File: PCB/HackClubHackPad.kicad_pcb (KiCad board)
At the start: 2 copper layers, 59.1 x 47 mm, 7 parts, among them J1 Conn_01x04, SW1 SW_Push, SW2 SW_Push, SW3 SW_Push, SW4 RotaryEncoder_Switch, SW5 RotaryEncoder_Switch, U1 Seeed Studio XIAO SAMD21

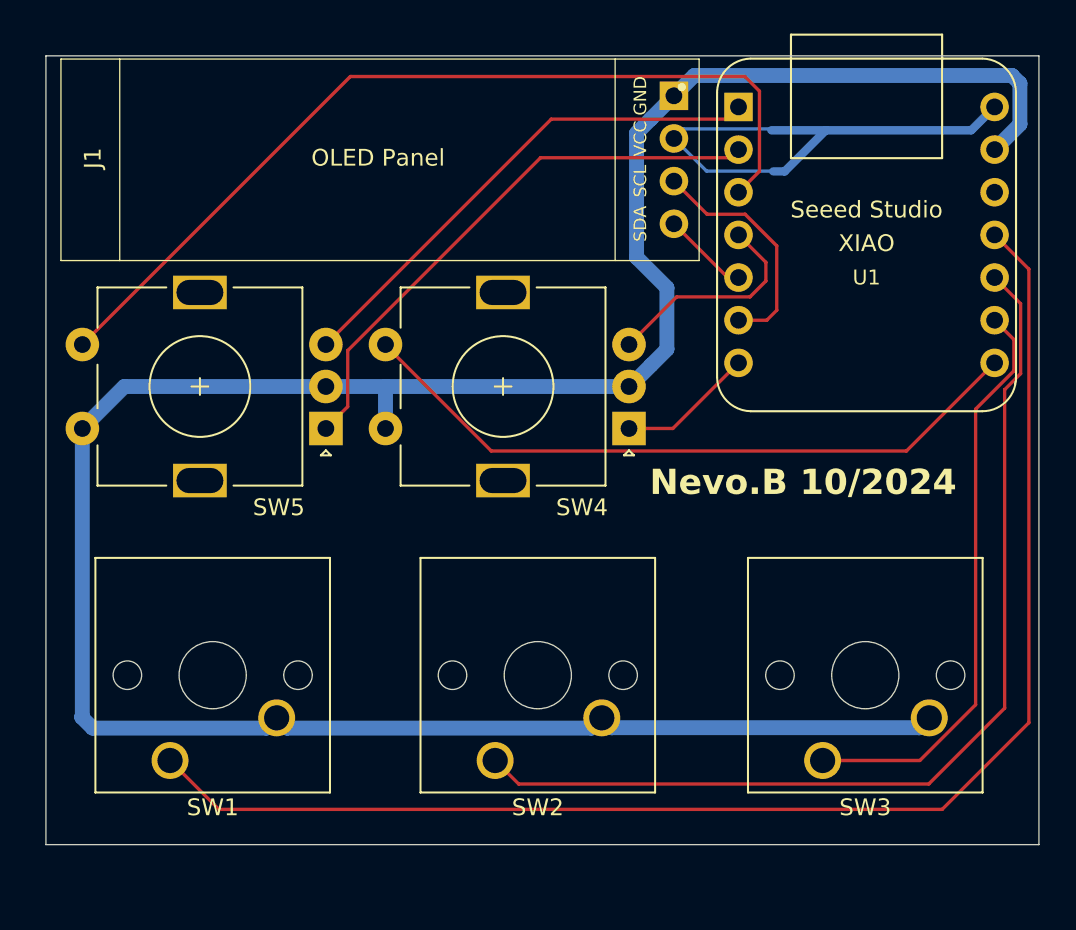
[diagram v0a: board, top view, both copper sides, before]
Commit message: Changed Board size and spacing
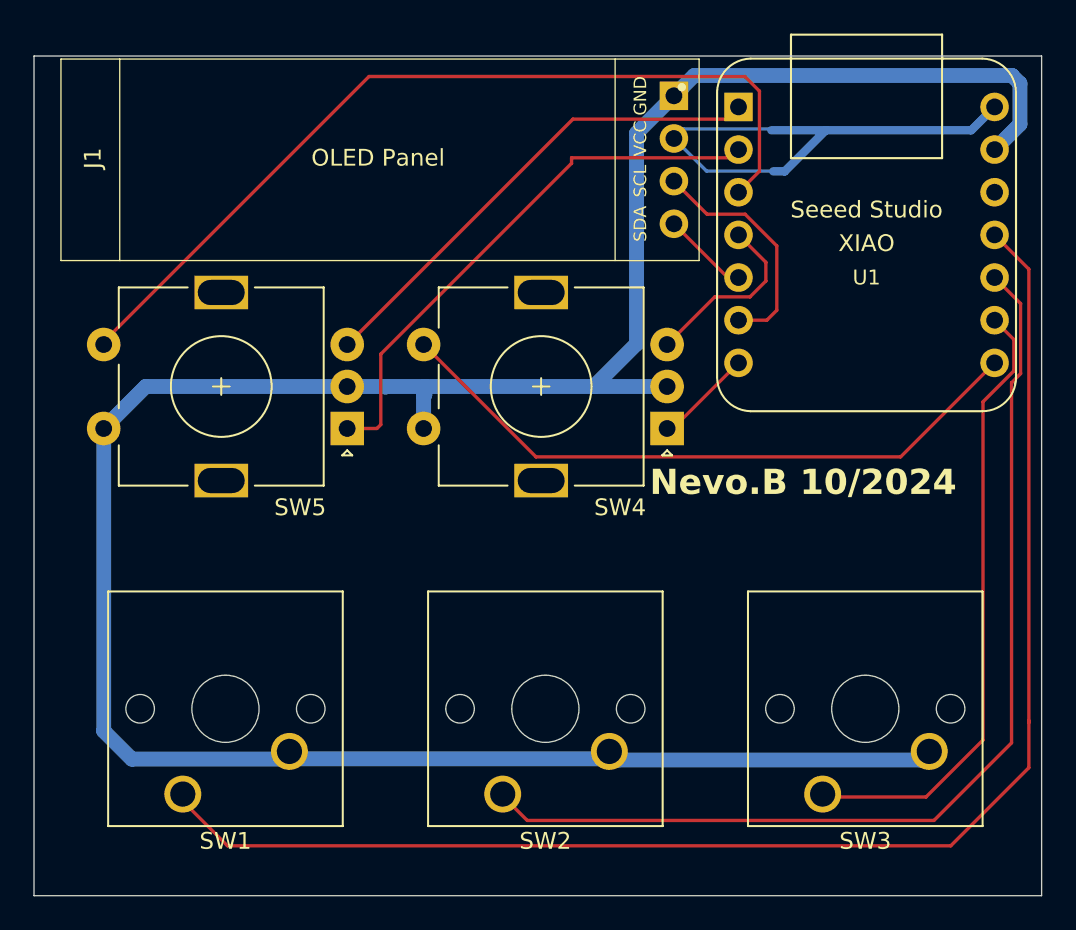
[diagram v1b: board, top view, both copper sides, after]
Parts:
- moved SW4 2.27 mm to (166.8, 45.0)
- moved SW1 2.14 mm to (137.9, 66.7)
- moved SW2 2.05 mm to (157.0, 66.7)
- moved SW3 2.00 mm to (176.0, 66.7)
- moved SW5 1.27 mm to (147.7, 45.0)
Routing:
- net Net-(U1-PB08_A6_D6_TX): track 8.14 -> 5.53 mm
- net Net-(U1-PA11_A3_D3): track 13.1 -> 10.9 mm
- net Net-(U1-PA6_A10_D10_MOSI): track 84.4 -> 86.5 mm
- net Net-(U1-PB09_A7_D7_RX): track 41.1 -> 39.0 mm
- net Net-(U1-PA7_A8_D8_SCK): track 34.8 -> 36.7 mm
- net Net-(U1-PA5_A9_D9_MISO): track 59.5 -> 61.3 mm
- net Net-(U1-PA02_A0_D0): track 30.4 -> 29.1 mm
- net Net-(U1-PA10_A2_D2): track 53.8 -> 52.7 mm
- net Net-(U1-PA4_A1_D1): track 33.4 -> 32.8 mm
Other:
- board size 59.1 x 47 mm -> 60 x 50 mm
